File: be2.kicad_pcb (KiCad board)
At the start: 2 copper layers, 35 parts, among them K1 mini_banana_jack, K2 mini_banana_jack, K3 mini_banana_jack, K4 mini_banana_jack, K5 mini_banana_jack, K6 mini_banana_jack, U1 AD620A, U2 TL082

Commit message: modifs
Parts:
- removed G***: LOGO, logo:logo_phelma_32x21mm
- removed R6, R7: 220k, Resistors_SMD:R_0805
- added C10: 10n, Capacitors_SMD:C_0805, F.Cu at (0.00, 0.00)
- added U3: TL082, Housings_SOIC:SOIC-8_3.9x4.9mm_Pitch1.27mm, F.Cu at (0.00, 0.00)
- C5: footprint Capacitors_SMD:C_0805 -> Capacitors_ThroughHole:C_Disc_D3_P2.5
- C8: value 20n -> 10n
- C9: value 20n -> 330n; footprint Capacitors_SMD:C_0805 -> Capacitors_ThroughHole:C_Disc_D3_P2.5
- R1: value 100K -> 270k
- R4, R5: value 220k -> 100K
- R8, R9: value 1k -> 10K
- moved D4 136.5 mm to (110.9, 79.6)
- moved D6 19.9 mm to (18.8, 6.57)
- moved D5 17.2 mm to (16.9, -2.96)
- moved R8 15.5 mm to (63.9, 94.2)
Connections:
- C5 pad 1: /mean_out -> GND
- C8 pad 1: Net-(C8-Pad1) -> GND
- C8 pad 2: /in+ -> VCC
- C9 pad 1: Net-(C9-Pad1) -> /mean_out
- C9 pad 2: /in- -> Net-(C9-Pad2)
- D1 pad 1: /u2_in- -> /u2_out
- D1 pad 2: /u2_out -> /u2_in-
- D2 pad 1: /u2_out -> /neg_out
- D2 pad 2: /neg_out -> /u2_out
- JP2 pad 1: /neg_out -> /neg_out_buff
- R4 pad 1: Net-(C5-Pad2) -> Net-(C9-Pad2)
- R5 pad 1: /mean_out -> Net-(C5-Pad2)
- R5 pad 2: Net-(C5-Pad2) -> Net-(C9-Pad2)
- R8 pad 1: Net-(C8-Pad1) -> /in+
- R9 pad 1: Net-(C9-Pad1) -> /in-
- U2 pad 5: GND -> /neg_out
- U2 pad 6: Net-(C5-Pad2) -> /neg_out_buff
- U2 pad 7: /mean_out -> /neg_out_buff
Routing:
- net GND: track 27.9 -> 32.1 mm

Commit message: we're routed, fall back!
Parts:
- removed K4, K5, K6: mini_banana_jack, lib:mini_banana_jack_2mm
- C1, C2: value 10u -> 1u; footprint Capacitors_ThroughHole:C_Radial_D5_L6_P2.5 -> Capacitors_SMD:C_1206
- C10, C3, C4, C6, C7, C8: footprint Capacitors_SMD:C_0805 -> Capacitors_SMD:C_1206
- C5, C9: footprint Capacitors_ThroughHole:C_Disc_D3_P2.5 -> Capacitors_SMD:C_1206
- D1, D2, D3, D4, D5, D6: footprint Diodes_ThroughHole:Diode_DO-35_SOD27_Horizontal_RM10 -> lib:Diode_DO-41_SOD81_Vertical_AnodeUp_phelma
- JP1, JP2: footprint Pin_Headers:Pin_Header_Straight_2x01 -> lib:JP_20mil
- K1: value mini_banana_jack -> CONN_01X03; footprint lib:mini_banana_jack_2mm -> lib:Pin_Header_Straight_1x03_phelma
- K2: value mini_banana_jack -> CONN_01X02; footprint lib:mini_banana_jack_2mm -> lib:Pin_Header_Straight_1x02_phelma
- K3: value mini_banana_jack -> CONN_01X01; footprint lib:mini_banana_jack_2mm -> lib:Pin_Header_Straight_1x01_phelma
- R1, R2, R3, R4, R5, R8, R9: footprint Resistors_SMD:R_0805 -> Resistors_SMD:R_1206
- moved C9 153.2 mm to (101.4, 114.9), turned to 90 degrees
- moved C8 150.8 mm to (95.0, 117.1)
- moved R9 150.2 mm to (86.5, 122.8)
- moved C10 149.9 mm to (100.9, 110.8)
- moved D5 147.2 mm to (93.1, 123.0), turned to 90 degrees
- moved U3 145.4 mm to (93.8, 111.1), turned to 180 degrees
- moved D6 133.1 mm to (90.1, 119.0), turned to 270 degrees
- moved K3 69.9 mm to (115.5, 108.8)
- moved K2 65.5 mm to (82.4, 121.5)
- moved C4 56.7 mm to (96.4, 130.0), turned to 270 degrees
- moved C3 56.2 mm to (100.5, 129.4), turned to 90 degrees
- moved U1 55.7 mm to (98.9, 124.3)
- moved R1 55.6 mm to (98.8, 120.2)
- moved K1 55.5 mm to (82.4, 111.3)
- moved C6 54.1 mm to (114.7, 127.3), turned to 90 degrees
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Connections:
- C1 pad 1: VCC -> GND
- C1 pad 2: GND -> VCC
- C2 pad 1: GND -> VSS
- C2 pad 2: VSS -> GND
- K1 pad 1: VCC -> GND
- K2 pad 1: GND -> /in-
- K3 pad 1: VSS -> /mean_out
- U3 pad 2: GND -> /mean_out
- U3 pad 5: GND -> /mean_out
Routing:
- net GND: track 32.1 -> 130.7 mm
- net VCC: track 20.8 -> 92.0 mm
- net VSS: track 67.8 -> 112.0 mm
- net /mean_out: track 0.00 -> 33.5 mm
- net /u2_in-: track 0.00 -> 23.5 mm
- net Net-(C5-Pad2): track 0.00 -> 14.2 mm
- net /u2_out: track 0.00 -> 14.0 mm
- net /mean_in: track 0.00 -> 12.8 mm
- net /neg_out: track 0.00 -> 11.3 mm
- net /neg_out_buff: track 0.00 -> 9.58 mm
- net Net-(C9-Pad2): track 0.00 -> 8.24 mm
- net /in+: track 10.4 -> 3.35 mm
- net /inf+: track 1.94 -> 8.87 mm
- net /diff_out: track 6.28 -> 10.6 mm
- net /inf-: track 4.94 -> 8.66 mm
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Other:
- board outline added: 50 x 30 mm
- net class Default: clearance 0.2 -> 0.3302; trace_width 0.4 -> 0.508
- net class power: clearance 0.4 -> 0.3302; trace_width 0.8 -> 0.762
- rule trace_clearance: 0.2 -> 0.3302
- rule trace_min: 0.2 -> 0.508

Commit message: cleaned up the pcb
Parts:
- moved C10 1.27 mm to (100.9, 109.6)
- moved C4 1.20 mm to (97.4, 129.4)
- moved C9 0.31 mm to (101.1, 114.8)
- moved R4 0.28 mm to (110.1, 112.0)
- moved R5 0.10 mm to (105.6, 112.0)
- turned C3 to 270 degrees
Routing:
- net GND: track 130.7 -> 124.4 mm
- net /mean_out: track 33.5 -> 32.3 mm
- net Net-(C5-Pad2): track 14.2 -> 13.1 mm
- net /mean_in: track 12.8 -> 12.0 mm
- net VCC: track 92.0 -> 91.3 mm
- net VSS: track 112.0 -> 111.4 mm

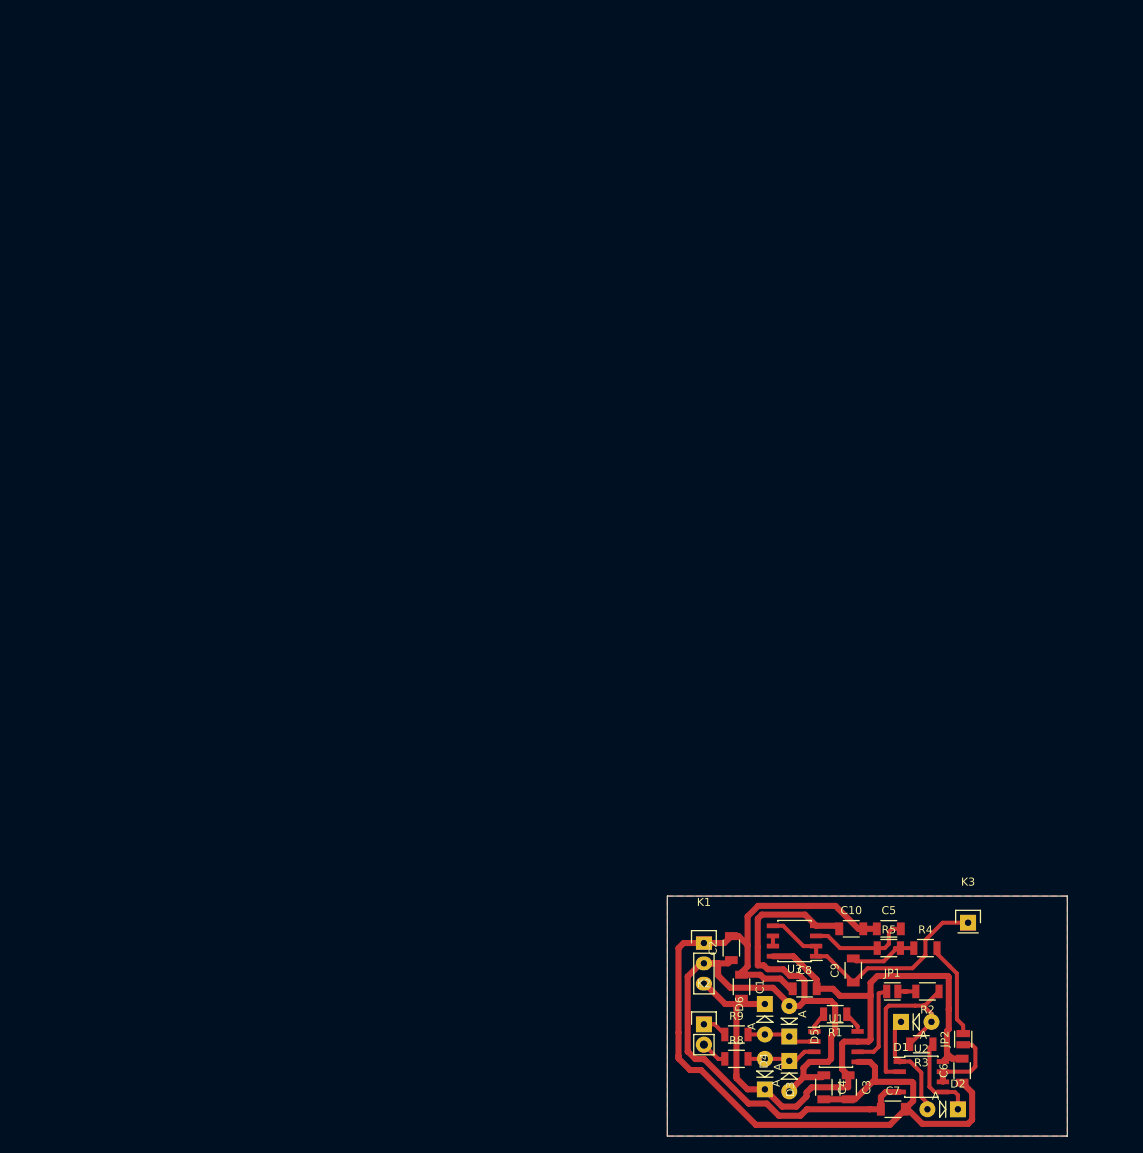
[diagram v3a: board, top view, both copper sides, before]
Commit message: through-hole components are now behind the pcb, connectors are aligned on a 0.1 inch grid
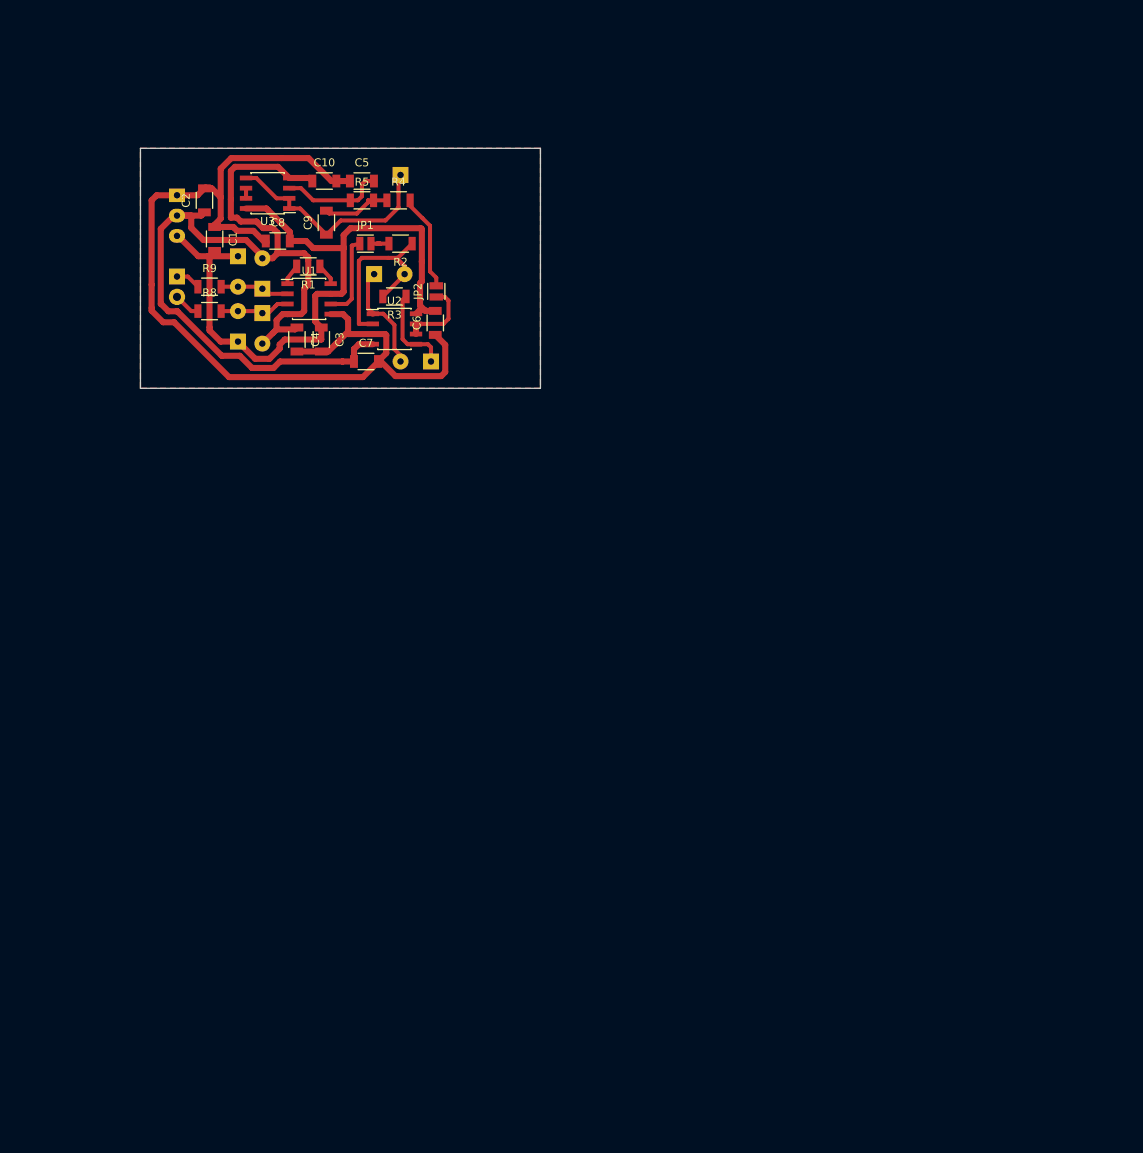
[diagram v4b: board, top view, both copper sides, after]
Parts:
- D1, D2, D3, D4, D5, D6, K1, K2, K3: moved to B.Cu
- moved K3 117.3 mm to (44.5, 15.3), turned to 180 degrees
- moved C1 114.3 mm to (21.3, 23.3)
- moved C10 114.3 mm to (35.0, 16.1)
- moved C2 114.3 mm to (20.0, 18.5)
- moved C3 114.3 mm to (34.6, 35.9)
- moved C4 114.3 mm to (31.6, 35.9)
- moved C5 114.3 mm to (39.7, 16.1)
- moved C6 114.3 mm to (48.9, 33.8)
- moved C8 114.3 mm to (29.2, 23.6)
- moved C9 114.3 mm to (35.2, 21.3)
- moved D1 114.3 mm to (41.2, 27.7)
- moved D3 114.3 mm to (24.2, 36.2)
- moved D4 114.3 mm to (27.2, 32.6)
- moved D5 114.3 mm to (27.2, 29.6)
- moved D6 114.3 mm to (24.2, 25.5)
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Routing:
- net /mean_out: track 32.3 -> 28.3 mm

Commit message: some cleaning on the pcb
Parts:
- moved U3 0.46 mm to (28.2, 18.0)
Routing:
- net VSS: track 111.4 -> 109.0 mm
- net GND: track 124.4 -> 123.0 mm
- net VCC: track 91.3 -> 90.7 mm

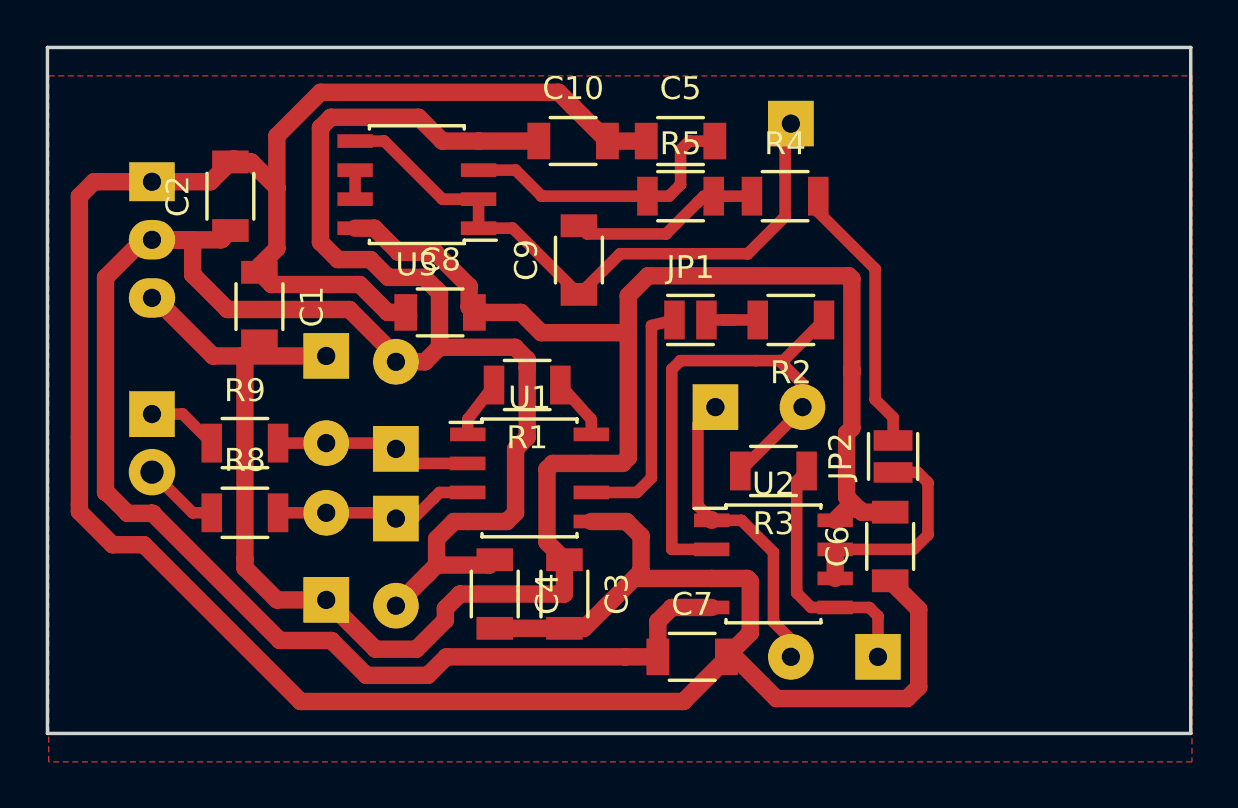
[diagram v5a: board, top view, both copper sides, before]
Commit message: IOs are now aligned on the same row
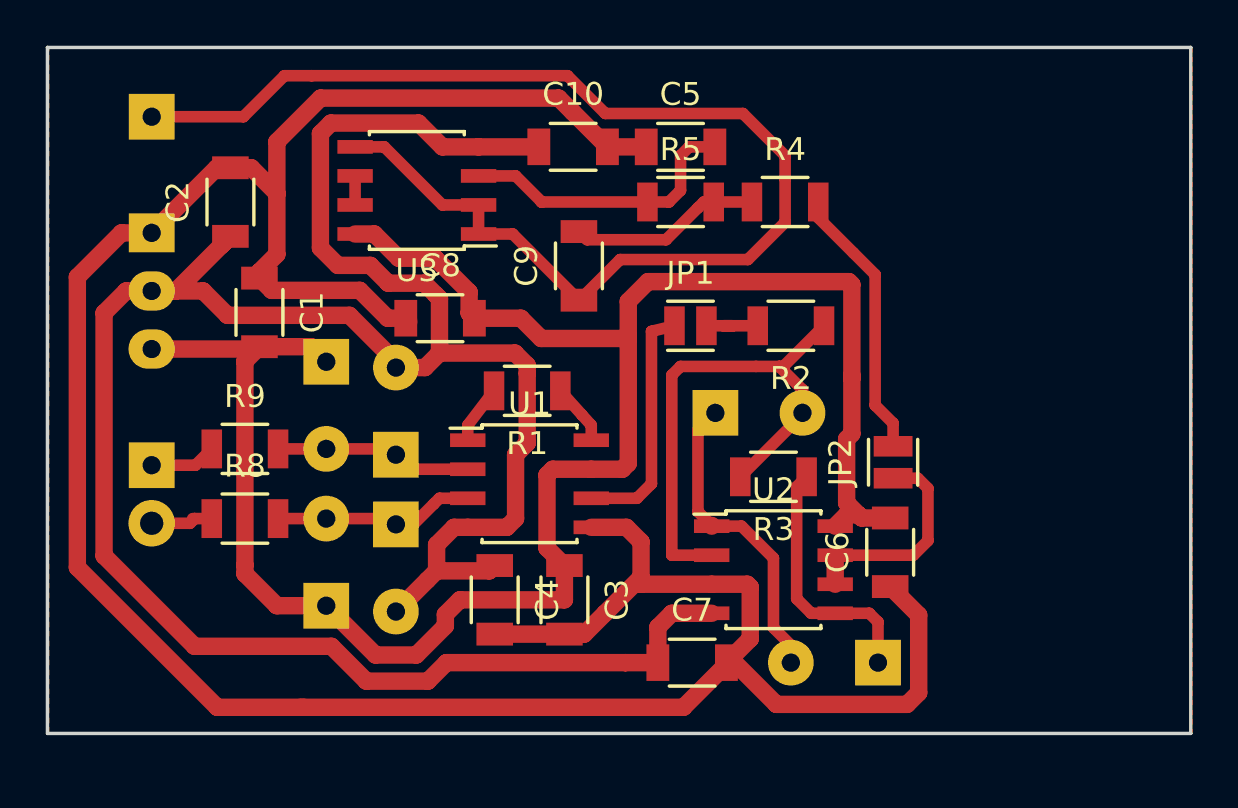
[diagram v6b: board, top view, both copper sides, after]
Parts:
- moved K3 28.0 mm to (16.6, 15.0)
- moved K1 2.24 mm to (16.6, 20.1)
- moved K2 2.24 mm to (16.6, 30.3)
- moved D3 0.25 mm to (24.2, 36.4)
- moved C1 0.25 mm to (21.3, 23.6)
- moved C2 0.25 mm to (20.0, 18.8)
- moved C5 0.25 mm to (39.7, 16.4)
- moved C9 0.25 mm to (35.2, 21.6)
- moved D5 0.25 mm to (27.2, 29.8)
- moved D6 0.25 mm to (24.2, 25.7)
- moved JP1 0.25 mm to (40.1, 24.2)
- moved JP2 0.25 mm to (49.0, 30.1)
- moved R2 0.25 mm to (44.5, 24.2)
- moved U3 0.25 mm to (28.2, 18.3)
- moved C10 0.25 mm to (35.0, 16.3)
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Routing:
- net /mean_out: track 27.9 -> 56.5 mm
- net VCC: track 90.7 -> 89.9 mm
- net GND: track 123.0 -> 122.4 mm
- net /in+: track 3.35 -> 2.80 mm

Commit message: part-1 : final plot in pdf
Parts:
- added G***: LOGO, logo:logo_phelma_32x21mm, F.Cu at (52.9, 19.3)
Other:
- board text added: "Lucien Dos Santos Farret Angelo Filippi 2016 PET-B"

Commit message: tiny correction
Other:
- board text added: "Dos Santos Farret Lucien Filippi Angelo 2016 PET-B"
- board text removed: "Lucien Dos Santos Farret Angelo Filippi 2016 PET-B"
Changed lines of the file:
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@@
 (kicad_pcb (version 4) (host pcbnew 0.201604021231+6659~43~ubuntu15.10.1-product)
   (general
-    (links 0)
+    (links 60)
     (no_connects 0)
     (area 9.5142 8.8435 118.666401 73.403601)
@@
       (xy 0.77232 -3.319656) (xy 0.909639 -3.431017) (xy 0.933808 -3.402492)) (layer F.Cu) (width 0.01))
   )
-  (gr_text "Lucien Dos Santos Farret\nAngelo Filippi 2016 PET-B" (at 58.981 40.4312 90) (layer F.Cu)
+  (gr_text "Dos Santos Farret Lucien\nFilippi Angelo 2016 PET-B" (at 58.981 40.4312 90) (layer F.Cu)
     (effects (font (size 0.9 0.9) (thickness 0.2)) (justify left))
   )
